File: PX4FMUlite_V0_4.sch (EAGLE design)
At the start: 128 parts, among them J2 DF13-4P-1.25V, J201 DF13C-6P-1.25V, J202 DF13C-6P-1.25V, J203 DF13C-6P-1.25V, J3 DF13C-4P-1.25V, J302 DF13C-4P-1.25V, J401 DF13C-4P-1.25V, J403 DF13C-7P-1.25V, J405 DF13C-4P-1.25V, J802 DF13C-3P-1.25V, M3_MOUNT1101 MOUNT-HOLE3.1MM, M3_MOUNT1102 MOUNT-HOLE3.1MM, M3_MOUNT1103 MOUNT-HOLE3.1MM, M3_MOUNT1104 MOUNT-HOLE3.1MM, U101 STM32F4X7VX, U2 MAX3051, U401 MAX3051, X101 3.2x2.5 mm / 24 MHz / 15 ppm

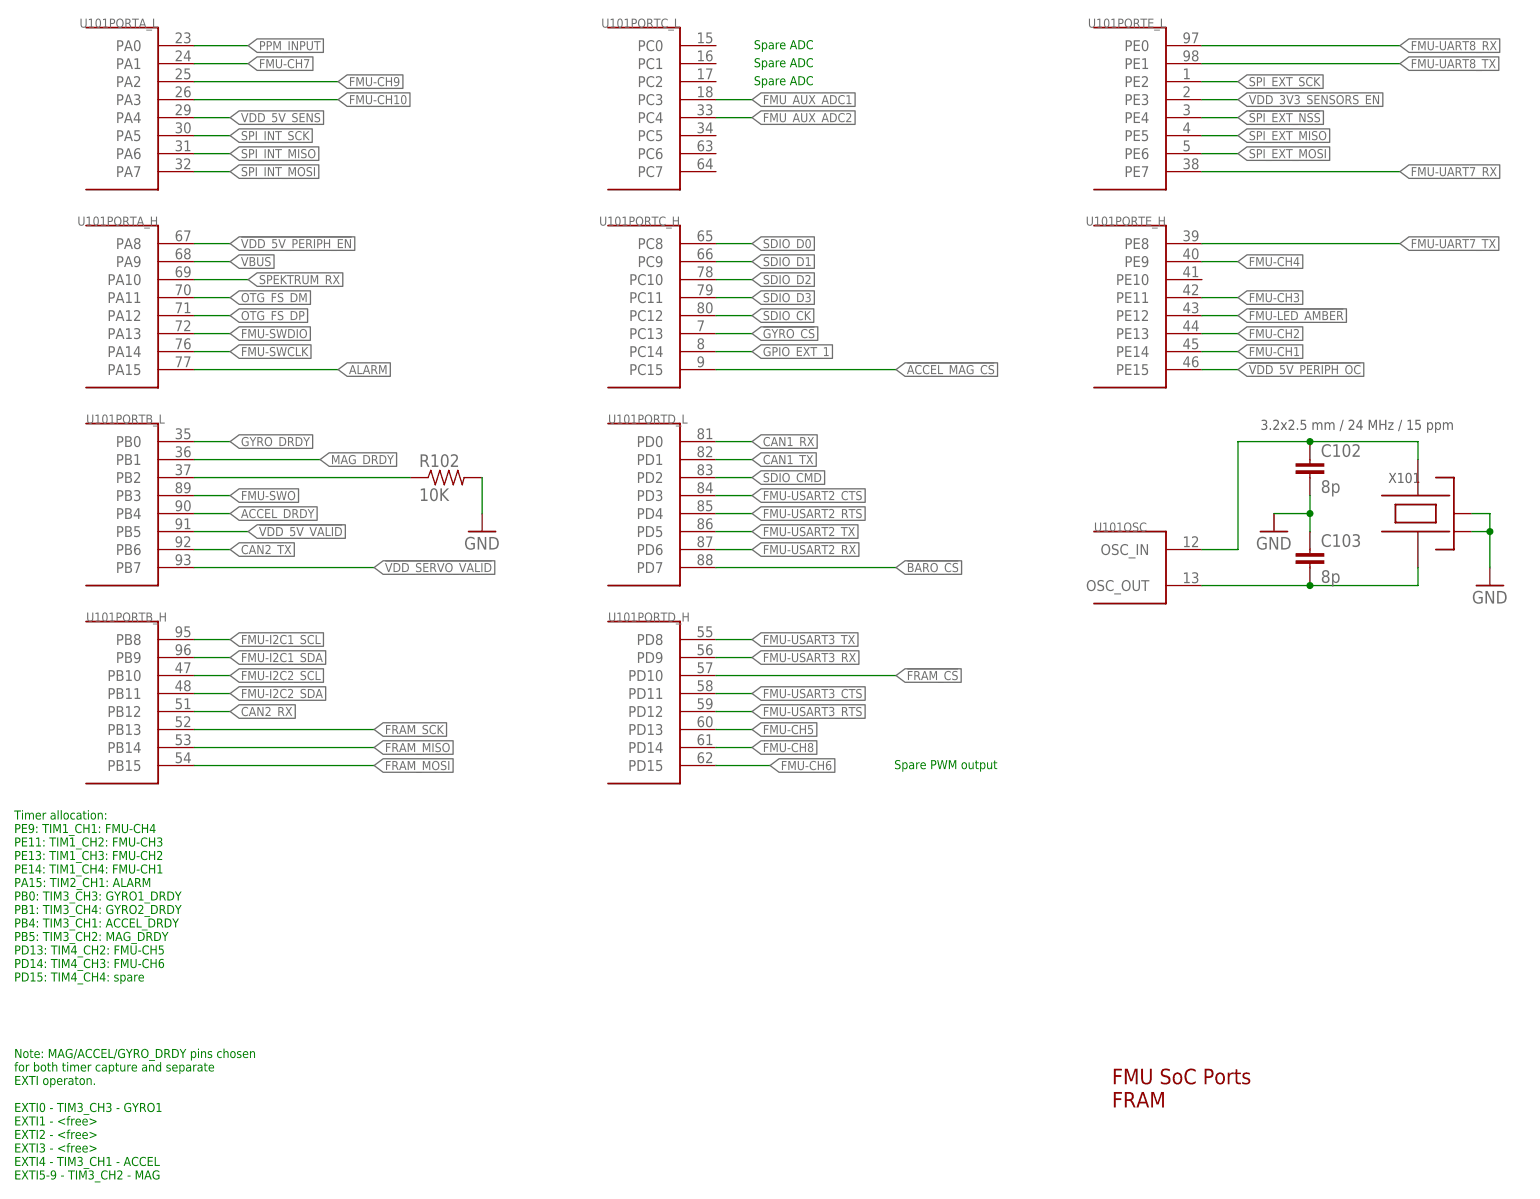
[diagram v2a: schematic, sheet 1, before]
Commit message: Everything fitted before autoroute
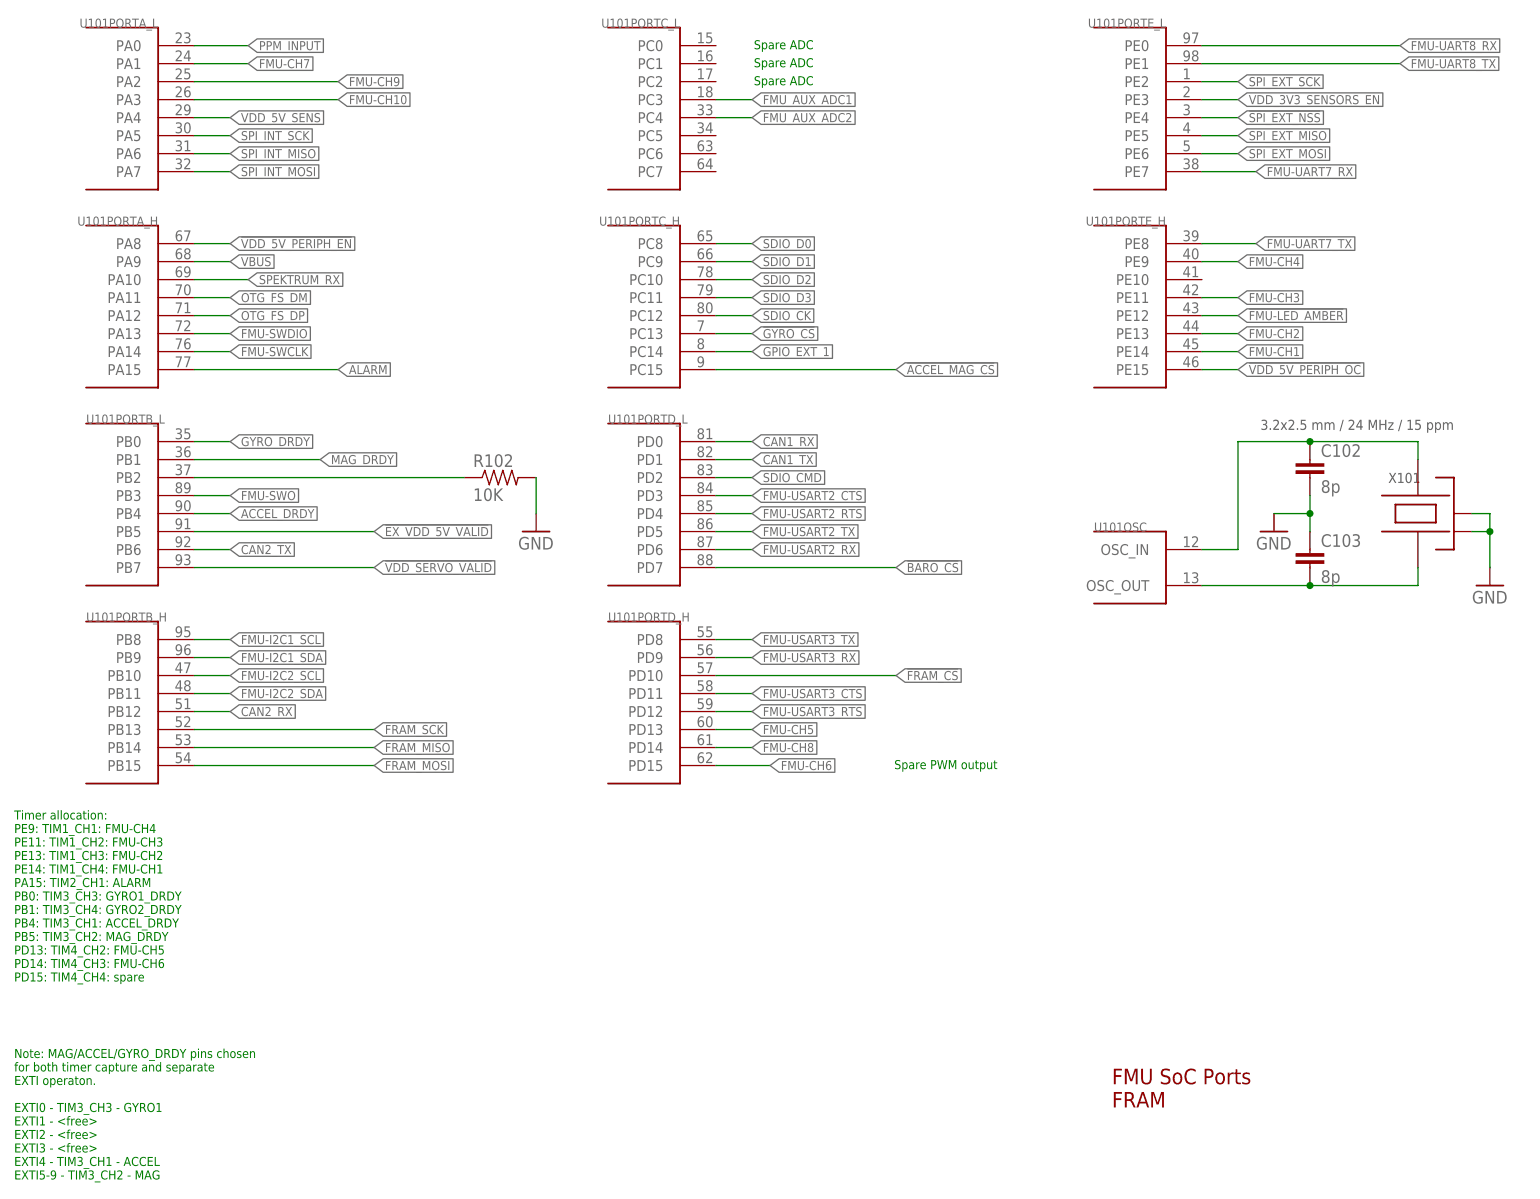
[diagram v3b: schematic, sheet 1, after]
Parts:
- removed R6: 10K, pixhawk2:RESISTOR0402-RES
- removed U$801: PESD0402-140, pixhawk2:DIODE-TVS
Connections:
- removed net !VDD_5V_VALID: R6.1, U$15.PG, U101PORTB_L.PB5
- new net !EX_VDD_5V_VALID: U101PORTB_L.PB5
- net GND: no longer U$801.A
- net VDD_3V3_SPEKTRUM: no longer U$801.C
- net VDD_5V: no longer R6.2
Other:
- note added: "REMOVED ESD PROTECTION, RELY ON OUTPUT CAPACITANCE"
- moved on the sheet: R102
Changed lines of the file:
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@@
 <attribute name="PARTNO" value="CC0402ZRY5V7BB104"/>
-</part>
-<part name="R6" library="pixhawk2" deviceset="RESISTOR" device="0402-RES" value="10K">
-<attribute name="PARTNO" value="RC0402FR-0710KL"/>
 </part>
 <part name="C7" library="pixhawk2" deviceset="CAP" device="0402" value="0u1">
@@
 </part>
 <part name="GND46" library="pixhawk2" deviceset="GND" device=""/>
-<part name="U$801" library="pixhawk2" deviceset="DIODE-TVS" device="" value="PESD0402-140">
-<attribute name="PARTNO" value="PESD0402-140"/>
-</part>
 <part name="U$14" library="PX4lite" deviceset="HEADER-3X1" device="RA"/>
 <part name="C13" library="pixhawk2" deviceset="CAP" device="0603" value="2u2">
@@
 </instance>
 <instance part="GND1" gate="1" x="185.42" y="96.52"/>
-<instance part="R102" gate="G$1" x="68.58" y="104.14">
-<attribute name="PARTNO" x="68.58" y="104.14" size="1.778" layer="96" display="off"/>
-</instance>
-<instance part="GND7" gate="1" x="73.66" y="96.52"/>
+<instance part="R102" gate="G$1" x="76.2" y="104.14">
+<attribute name="PARTNO" x="76.2" y="104.14" size="1.778" layer="96" display="off"/>
+</instance>
+<instance part="GND7" gate="1" x="81.28" y="96.52"/>
 <instance part="GND11" gate="1" x="215.9" y="88.9"/>
 <instance part="FRAME1" gate="G$1" x="0" y="0"/>
@@
 <net name="PB2-BOOT1" class="0">
 <segment>
-<wire x1="33.02" y1="104.14" x2="63.5" y2="104.14" width="0.1524" layer="91"/>
+<wire x1="33.02" y1="104.14" x2="71.12" y2="104.14" width="0.1524" layer="91"/>
 <pinref part="R102" gate="G$1" pin="1"/>
 <pinref part="U101" gate="PORTB_L" pin="PB2"/>
@@
 </segment>
 <segment>
-<wire x1="73.66" y1="99.06" x2="73.66" y2="104.14" width="0.1524" layer="91"/>
+<wire x1="81.28" y1="99.06" x2="81.28" y2="104.14" width="0.1524" layer="91"/>
 <pinref part="GND7" gate="1" pin="GND"/>
 <pinref part="R102" gate="G$1" pin="2"/>
@@
 <segment>
 <pinref part="U101" gate="PORTE_L" pin="PE7"/>
-<wire x1="175.26" y1="147.32" x2="203.2" y2="147.32" width="0.1524" layer="91"/>
-<label x="203.2" y="147.32" size="1.27" layer="95" xref="yes"/>
+<wire x1="175.26" y1="147.32" x2="182.88" y2="147.32" width="0.1524" layer="91"/>
+<label x="182.88" y="147.32" size="1.27" layer="95" xref="yes"/>
 </segment>
 </net>
@@
 <segment>
 <pinref part="U101" gate="PORTE_H" pin="PE8"/>
-<wire x1="175.26" y1="137.16" x2="203.2" y2="137.16" width="0.1524" layer="91"/>
-<label x="203.2" y="137.16" size="1.27" layer="95" xref="yes"/>
+<wire x1="175.26" y1="137.16" x2="182.88" y2="137.16" width="0.1524" layer="91"/>
+<label x="182.88" y="137.16" size="1.27" layer="95" xref="yes"/>
 </segment>
 </net>
@@
 </segment>
 </net>
-<net name="!VDD_5V_VALID" class="0">
+<net name="!EX_VDD_5V_VALID" class="0">
 <segment>
 <pinref part="U101" gate="PORTB_L" pin="PB5"/>
-<wire x1="33.02" y1="96.52" x2="40.64" y2="96.52" width="0.1524" layer="91"/>
-<label x="40.64" y="96.52" size="1.27" layer="95" xref="yes"/>
+<wire x1="33.02" y1="96.52" x2="58.42" y2="96.52" width="0.1524" layer="91"/>
+<label x="58.42" y="96.52" size="1.27" layer="95" xref="yes"/>
 </segment>
 </net>
@@
 <text x="231.14" y="78.74" size="1.778" layer="95">Default GPS port</text>
 <text x="53.34" y="88.9" size="1.778" layer="97">Spektrum/DSM</text>
+<text x="58.42" y="68.58" size="1.778" layer="91">REMOVED ESD PROTECTION,
+RELY ON OUTPUT CAPACITANCE</text>
 </plain>
 <instances>
@@
 <instance part="GND9" gate="1" x="45.72" y="20.32"/>
 <instance part="GND46" gate="1" x="81.28" y="60.96"/>
-<instance part="U$801" gate="G$1" x="81.28" y="71.12" rot="R90">
-<attribute name="PARTNO" x="81.28" y="71.12" size="1.778" layer="96" display="off"/>
-</instance>
 <instance part="U$14" gate="G$1" x="114.3" y="78.74"/>
 <instance part="L3" gate="G$1" x="83.82" y="30.48"/>
@@
 <segment>
 <pinref part="GND46" gate="1" pin="GND"/>
-<pinref part="U$801" gate="G$1" pin="A"/>
-<wire x1="81.28" y1="68.58" x2="81.28" y2="66.04" width="0.1524" layer="91"/>
 <pinref part="U$14" gate="G$1" pin="3"/>
 <wire x1="81.28" y1="66.04" x2="81.28" y2="63.5" width="0.1524" layer="91"/>
@@
 <wire x1="104.14" y1="78.74" x2="104.14" y2="66.04" width="0.1524" layer="91"/>
 <wire x1="104.14" y1="66.04" x2="81.28" y2="66.04" width="0.1524" layer="91"/>
-<junction x="81.28" y="66.04"/>
 </segment>
 </net>
@@
 <segment>
 <label x="73.66" y="81.28" size="1.27" layer="95" rot="R180" xref="yes"/>
-<pinref part="U$801" gate="G$1" pin="C"/>
-<wire x1="81.28" y1="81.28" x2="73.66" y2="81.28" width="0.1524" layer="91"/>
-<wire x1="81.28" y1="73.66" x2="81.28" y2="81.28" width="0.1524" layer="91"/>
 <pinref part="U$14" gate="G$1" pin="2"/>
-<wire x1="106.68" y1="81.28" x2="81.28" y2="81.28" width="0.1524" layer="91"/>
-<junction x="81.28" y="81.28"/>
+<wire x1="106.68" y1="81.28" x2="73.66" y2="81.28" width="0.1524" layer="91"/>
 </segment>
 </net>
@@
 <instance part="C6" gate="G$1" x="68.58" y="93.98">
 <attribute name="PARTNO" x="68.58" y="93.98" size="1.778" layer="96" display="off"/>
-</instance>
-<instance part="R6" gate="G$1" x="182.88" y="111.76" rot="R90">
-<attribute name="PARTNO" x="182.88" y="111.76" size="1.778" layer="96" display="off"/>
 </instance>
 <instance part="C7" gate="G$1" x="139.7" y="111.76">
@@
 </segment>
 </net>
-<net name="!VDD_5V_VALID" class="0">
-<segment>
-<label x="190.5" y="104.14" size="1.27" layer="95" xref="yes"/>
-<pinref part="U$15" gate="A" pin="PG"/>
-<wire x1="190.5" y1="104.14" x2="182.88" y2="104.14" width="0.1524" layer="91"/>
-<pinref part="R6" gate="G$1" pin="1"/>
-<wire x1="182.88" y1="104.14" x2="121.92" y2="104.14" width="0.1524" layer="91"/>
-<wire x1="182.88" y1="106.68" x2="182.88" y2="104.14" width="0.1524" layer="91"/>
-<junction x="182.88" y="104.14"/>
-</segment>
-</net>
 <net name="VDD_5V" class="1">
 <segment>
@@
 <pinref part="C9" gate="G$1" pin="1"/>
 <wire x1="147.32" y1="116.84" x2="147.32" y2="121.92" width="0.1524" layer="91"/>
-<wire x1="167.64" y1="121.92" x2="182.88" y2="121.92" width="0.1524" layer="91"/>
+<wire x1="167.64" y1="121.92" x2="190.5" y2="121.92" width="0.1524" layer="91"/>
 <label x="190.5" y="121.92" size="1.27" layer="95" xref="yes"/>
 <junction x="167.64" y="121.92"/>
 <junction x="147.32" y="121.92"/>
 <junction x="157.48" y="121.92"/>
-<pinref part="R6" gate="G$1" pin="2"/>
-<wire x1="182.88" y1="121.92" x2="190.5" y2="121.92" width="0.1524" layer="91"/>
-<wire x1="182.88" y1="116.84" x2="182.88" y2="121.92" width="0.1524" layer="91"/>
-<junction x="182.88" y="121.92"/>
 <pinref part="C7" gate="G$1" pin="1"/>
 <wire x1="139.7" y1="116.84" x2="139.7" y2="121.92" width="0.1524" layer="91"/>
